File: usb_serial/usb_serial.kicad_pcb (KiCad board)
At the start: 2 copper layers, 3 parts, among them J1 47589-1001, J3 Conn_01x04_Pin, U1 FT232RL

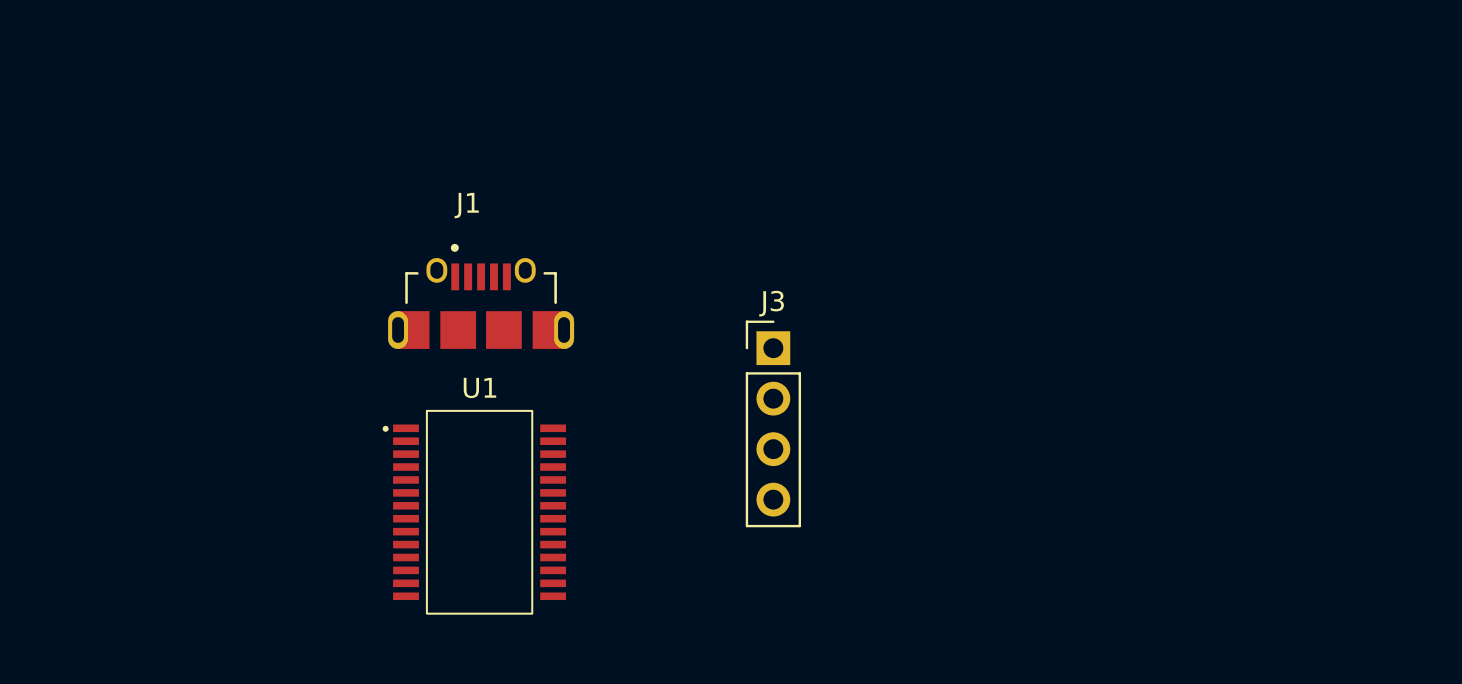
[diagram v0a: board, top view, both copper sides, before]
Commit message: Board outline defined
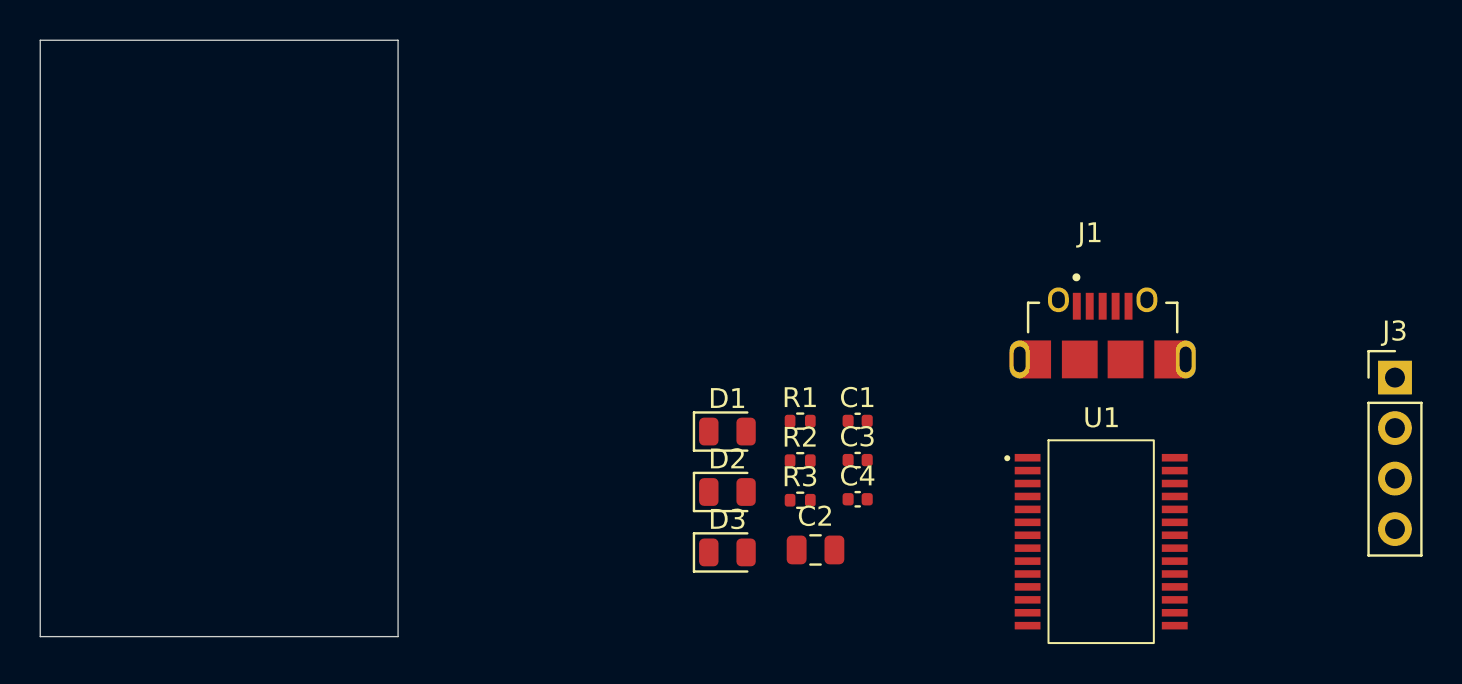
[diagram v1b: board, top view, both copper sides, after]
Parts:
- added C1: 10n, Capacitor_SMD:C_0402_1005Metric, F.Cu at (171.1, 79.2)
- added C2: 4.7u, Capacitor_SMD:C_0805_2012Metric, F.Cu at (169.0, 85.6)
- added C3: 100n, Capacitor_SMD:C_0402_1005Metric, F.Cu at (171.1, 81.1)
- added C4: 100n, Capacitor_SMD:C_0402_1005Metric, F.Cu at (171.1, 83.1)
- added D1: LED, LED_SMD:LED_0805_2012Metric, F.Cu at (164.6, 79.7)
- added D2: LED, LED_SMD:LED_0805_2012Metric, F.Cu at (164.6, 82.7)
- added D3: LED, LED_SMD:LED_0805_2012Metric, F.Cu at (164.6, 85.8)
- added R1: 1k, Resistor_SMD:R_0402_1005Metric, F.Cu at (168.2, 79.2)
- added R2: 1k, Resistor_SMD:R_0402_1005Metric, F.Cu at (168.2, 81.2)
- added R3: 2.2k, Resistor_SMD:R_0402_1005Metric, F.Cu at (168.2, 83.1)
- moved J3 31.3 mm to (198.2, 77.0)
- moved U1 31.3 mm to (183.4, 85.2)
- moved J1 31.3 mm to (183.4, 76.4)
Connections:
- J1 pad 1: unconnected-(J1-VBUS-Pad1) -> +5V
- J1 pad 2: unconnected-(J1-D--Pad2) -> /USB_DN
- J1 pad 3: unconnected-(J1-D+-Pad3) -> /USB_DP
- J1 pad 5: unconnected-(J1-GND-Pad5) -> GND
- J1 pad SH1: Net-(J1-SHIELD-PadSH1) -> GND
- J1 pad SH2: Net-(J1-SHIELD-PadSH1) -> GND
- J1 pad SH3: Net-(J1-SHIELD-PadSH1) -> GND
- J1 pad SH4: Net-(J1-SHIELD-PadSH1) -> GND
- J1 pad SH5: Net-(J1-SHIELD-PadSH1) -> GND
- J1 pad SH6: Net-(J1-SHIELD-PadSH1) -> GND
- J3 pad 1: unconnected-(J3-Pin_1-Pad1) -> +5V
- J3 pad 2: unconnected-(J3-Pin_2-Pad2) -> /UART_TX
- J3 pad 3: unconnected-(J3-Pin_3-Pad3) -> /UART_RX
- J3 pad 4: unconnected-(J3-Pin_4-Pad4) -> GND
- U1 pad 1: unconnected-(U1-TXD-Pad1) -> /UART_TX
- U1 pad 15: unconnected-(U1-USBDP-Pad15) -> /USB_DP
- U1 pad 16: unconnected-(U1-USBDM-Pad16) -> /USB_DN
- U1 pad 17: unconnected-(U1-3V3OUT-Pad17) -> +3.3V
- U1 pad 18: unconnected-(U1-GND-Pad18) -> GND
- U1 pad 20: unconnected-(U1-VCC-Pad20) -> +5V
- U1 pad 21: unconnected-(U1-GND-Pad21) -> GND
- U1 pad 25: unconnected-(U1-AGND-Pad25) -> GND
- U1 pad 26: unconnected-(U1-TEST-Pad26) -> GND
- U1 pad 4: unconnected-(U1-VCCIO-Pad4) -> +3.3V
- U1 pad 5: unconnected-(U1-RXD-Pad5) -> /UART_RX
- U1 pad 7: unconnected-(U1-GND-Pad7) -> GND
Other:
- board outline added: 18 x 30 mm

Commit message: Placement done
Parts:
- moved J3 63.8 mm to (135.2, 87.4), turned to 90 degrees
- moved J1 47.0 mm to (139.0, 61.2), turned to 180 degrees
- moved U1 45.6 mm to (139.0, 74.5)
- moved R2 39.3 mm to (131.8, 66.4), turned to 180 degrees
- moved R1 36.4 mm to (131.8, 77.3), turned to 180 degrees
- moved D2 35.5 mm to (131.8, 69.1), turned to -90 degrees
- moved D1 32.7 mm to (131.8, 80.0), turned to -90 degrees
- moved C1 30.3 mm to (143.5, 66.7)
- moved D3 29.7 mm to (146.2, 62.4), turned to 90 degrees
- moved R3 27.5 mm to (146.2, 66.6), turned to 180 degrees
- moved C2 26.5 mm to (145.5, 73.3), turned to 90 degrees
- moved C3 26.2 mm to (145.5, 75.6)
- moved C4 26.1 mm to (145.5, 78.4)
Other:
- board text added: "5v"
- board text added: "GND"
- board text added: "RX"
- board text added: "TX"

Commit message: Cooper fill + USB connector footprint change
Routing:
- added copper zone on B.Cu, net GND
- added copper zone on F.Cu, net GND

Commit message: Routing done
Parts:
- moved C4 0.66 mm to (145.0, 78.9), turned to -90 degrees
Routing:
- net +5V: track 0.00 -> 50.2 mm, vias 0 -> 2
- net +3.3V: track 0.00 -> 38.7 mm
- net /UART_RX: track 0.00 -> 28.2 mm, vias 0 -> 1
- net /UART_TX: track 0.00 -> 21.1 mm, vias 0 -> 1
- net /USB_DP: track 0.00 -> 17.5 mm
- net /USB_DN: track 0.00 -> 16.8 mm
- net GND: track 0.00 -> 11.7 mm, vias 0 -> 9
- net Net-(D3-K): track 0.00 -> 3.54 mm
- net Net-(D2-K): track 0.00 -> 1.97 mm
- net Net-(D1-K): track 0.00 -> 1.97 mm
